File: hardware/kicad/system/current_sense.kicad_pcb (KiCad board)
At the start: 2 copper layers, 134 x 58 mm, 17 parts, among them J1 kanal 1 retur, J2 kanal 2 retur, J3 kanal 3 retur, J4 Arduino, U1 LM358, U2 LM358

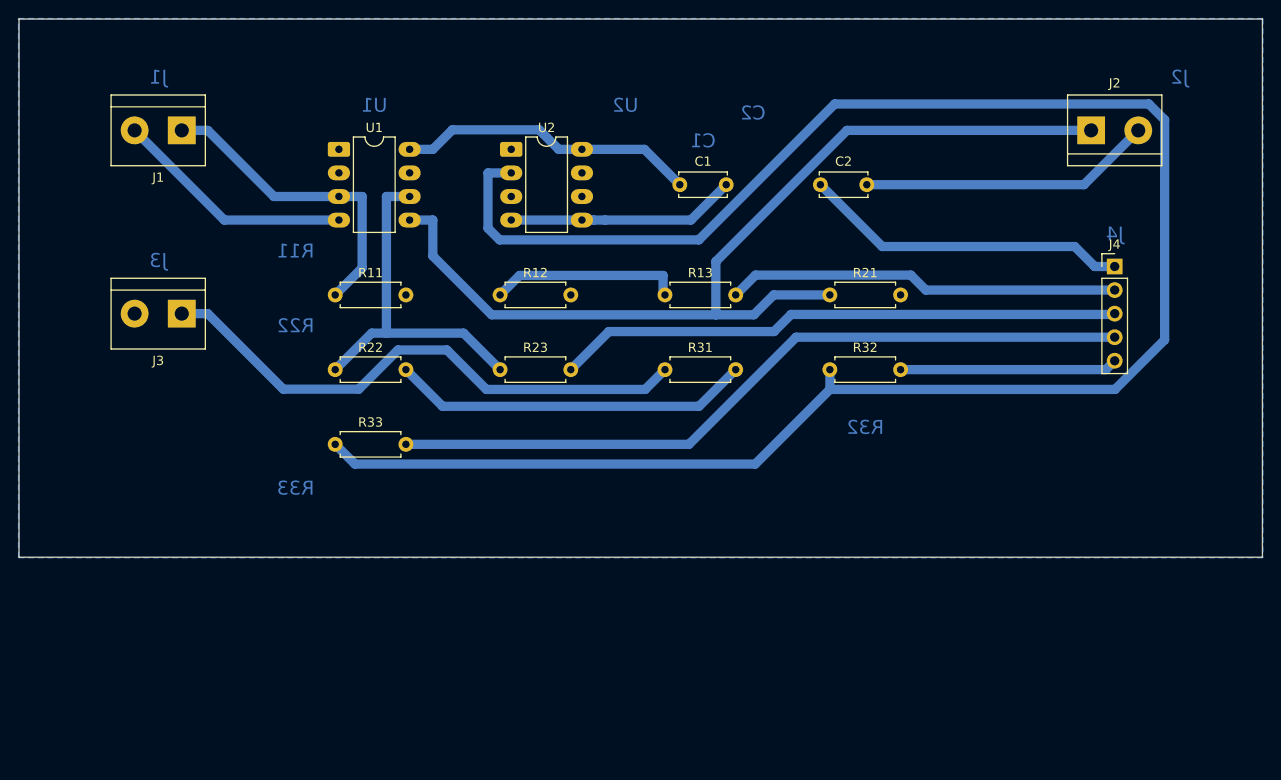
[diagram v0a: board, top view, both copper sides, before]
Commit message: Hand-place mppt and current_sense following the signal flow
The auto-grid placement scattered the per-channel parts and starved the
single-layer router: current_sense had 15 airwires (a third of the
board hand-wired) and mppt 10. pcb_build.py now takes an explicit
placement table for these two - channels run left to right (terminal ->
shunt -> gain pair -> op-amp -> header), PV chain likewise - and the
boards shrank in the process (mppt 165x82 -> 140x68, current_sense
134x58 -> 120x80).

Jumpers now: mppt 7, current_sense 10, both DRC-clean (one cosmetic
silk-over-mask warning on mppt; silk isn't part of the laser flow).
Also fixed in this pass: shunt pair R5/R6 flipped so same-net pads
face each other, and a local 'import json' that shadowed the module
import and broke pcb_build entirely. Production DXF/gerbers re-exported,
cut sizes and jumper tables updated.
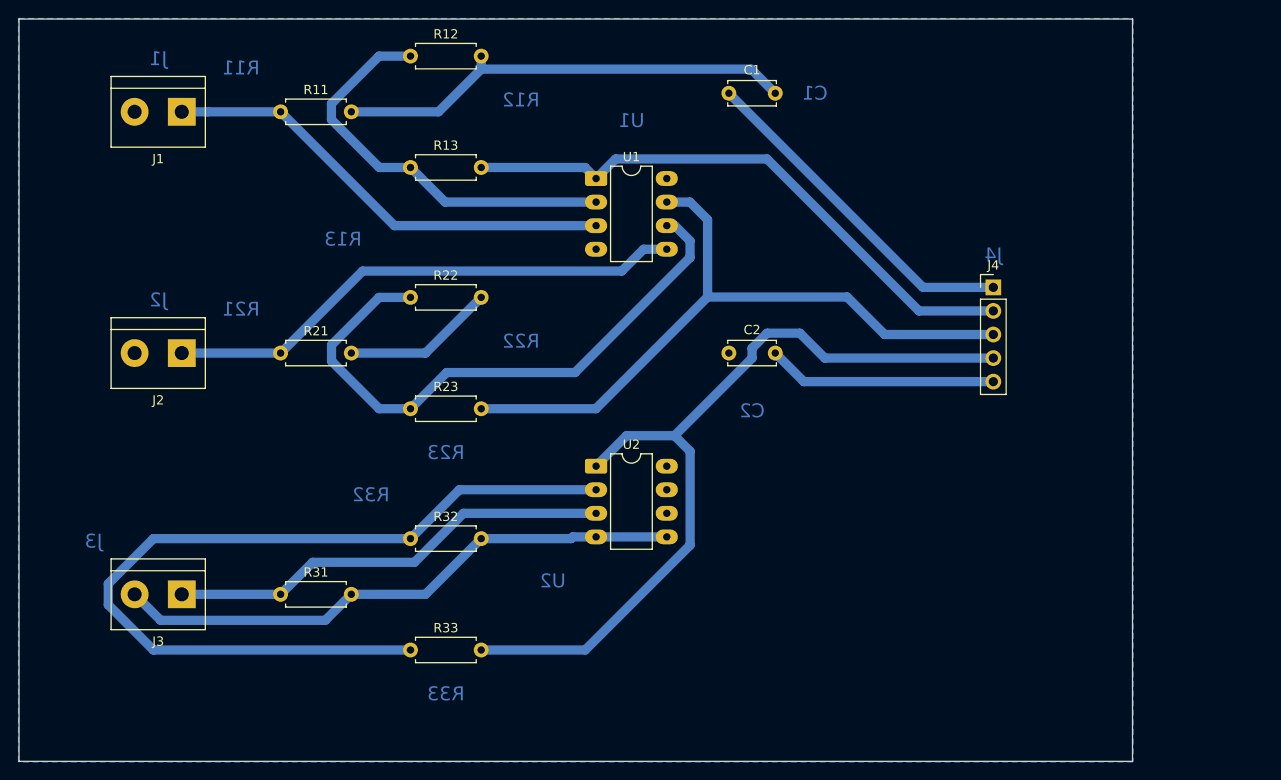
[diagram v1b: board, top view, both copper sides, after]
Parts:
- moved J2 100.9 mm to (37.5, 56.0), turned to 180 degrees
- moved R21 59.5 mm to (48.2, 56.0)
- moved R32 48.7 mm to (62.2, 76.0)
- moved R31 48.0 mm to (48.2, 82.0)
- moved U2 35.3 mm to (82.2, 68.2)
- moved R13 30.7 mm to (62.2, 36.0)
- moved J3 30.2 mm to (37.5, 82.0)
- moved U1 27.9 mm to (82.2, 37.2)
- moved R12 27.5 mm to (62.2, 24.0)
- moved R33 23.6 mm to (62.2, 88.0)
- moved C2 20.7 mm to (96.5, 56.0)
- moved R11 20.6 mm to (48.2, 30.0)
- moved J4 13.3 mm to (125.0, 48.9)
- moved R22 11.2 mm to (62.2, 50.0)
- moved C1 11.2 mm to (96.5, 28.0)
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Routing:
- net /FB3: track 210.3 -> 93.6 mm
- net /RET2: track 104.7 -> 56.9 mm
- net +5V: track 67.8 -> 37.2 mm
- net /FB2: track 38.3 -> 64.9 mm
- net /FB1: track 20.6 -> 44.6 mm
- net /I_SENSE1: track 42.4 -> 63.3 mm
- net /RET1: track 34.2 -> 49.7 mm
- net /I_SENSE2: track 61.1 -> 75.4 mm
- net /RET3: track 59.8 -> 48.3 mm
- net /I_SENSE3: track 81.2 -> 90.2 mm
- net GND: track 144.7 -> 153.6 mm
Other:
- board size 134 x 58 mm -> 120 x 80 mm
- board text added: "R12"
- board text added: "R13"
- board text added: "R21"
- board text added: "R23"
